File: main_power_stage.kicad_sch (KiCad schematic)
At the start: 67 parts, among them SW1 CAS-120TA, U2 LV14540DDAR, U6 TPS65987DDHRSHR, U7 LV14540DDAR, U8 74CBTLV3257_VQFN, U9 W25Q80DV_SOIC-8

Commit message: [#62623] Minor graphical changes
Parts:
- added R63: R_0R_0402, antmicro-footprints:R_0402_1005Metric, symbol antmicroResistors0402:R_0R_0402
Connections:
- net FTDI_TPS_rst: now also R63.1; no longer R32.2, U6.44 (HRESET)
- new net PDC_RESET: R32.2, R63.2, U6.44 (HRESET)
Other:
- moved on the sheet: R57, U8

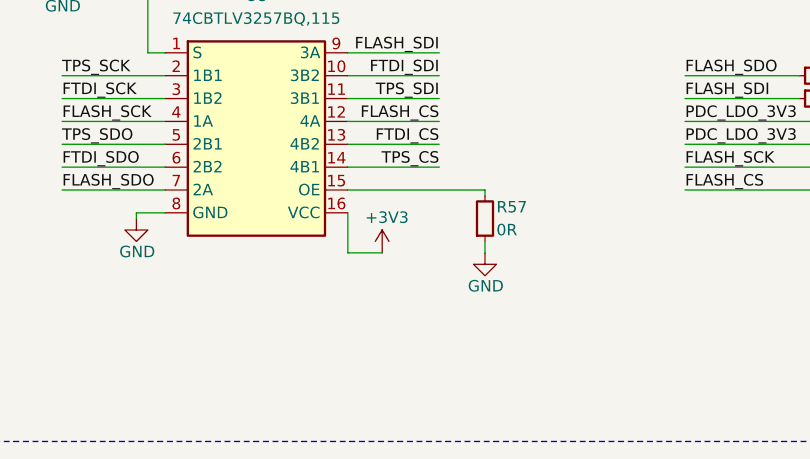
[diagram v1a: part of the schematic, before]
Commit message: [#62623] PCB initial placement
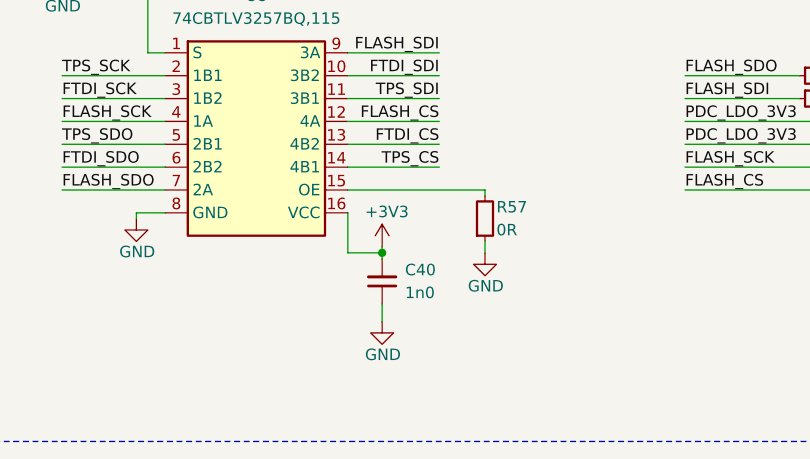
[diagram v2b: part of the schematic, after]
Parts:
- added C40: C_1n0_0402, antmicro-footprints:C_0402_1005Metric, symbol antmicroCapacitors0402:C_1n0_0402
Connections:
- net +3V3: now also C40.2
- net GND: now also C40.1
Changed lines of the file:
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@@
   (junction (at 154.305 92.71) (diameter 0) (color 0 0 0 0)
   )
+  (junction (at 147.32 263.525) (diameter 0) (color 0 0 0 0)
+  )
   (junction (at 247.65 96.52) (diameter 0) (color 0 0 0 0)
   )
@@
     (stroke (width 0) (type default))
   )
+  (wire (pts (xy 147.32 263.525) (xy 147.32 262.89))
+    (stroke (width 0) (type default))
+  )
   (wire (pts (xy 93.345 33.02) (xy 97.79 33.02))
     (stroke (width 0) (type default))
@@
     (stroke (width 0) (type default))
   )
-  (wire (pts (xy 143.51 259.08) (xy 143.51 263.525))
-    (stroke (width 0) (type default))
-  )
   (wire (pts (xy 257.81 96.52) (xy 261.62 96.52))
     (stroke (width 0) (type default))
@@
     (stroke (width 0) (type default))
   )
+  (wire (pts (xy 143.51 259.08) (xy 143.51 263.525))
+    (stroke (width 0) (type default))
+  )
   (wire (pts (xy 97.79 38.1) (xy 102.235 38.1))
     (stroke (width 0) (type default))
@@
     (stroke (width 0) (type default))
   )
+  (wire (pts (xy 143.51 263.525) (xy 147.32 263.525))
+    (stroke (width 0) (type default))
+  )
   (wire (pts (xy 252.73 69.215) (xy 252.73 70.485))
     (stroke (width 0) (type default))
@@
     (stroke (width 0) (type default))
   )
-  (wire (pts (xy 143.51 263.525) (xy 147.32 263.525))
+  (wire (pts (xy 147.32 264.16) (xy 147.32 263.525))
     (stroke (width 0) (type default))
   )
@@
     (stroke (width 0) (type default))
   )
+  (wire (pts (xy 147.32 269.24) (xy 147.32 271.145))
+    (stroke (width 0) (type default))
+  )
   (wire (pts (xy 128.27 152.4) (xy 128.27 154.94))
     (stroke (width 0) (type default))
@@
     (effects (font (size 1.27 1.27)) (justify right bottom))
   )
-  (label "SCL" (at 398.78 39.37 180)
+  (label "SCL" (at 398.78 39.37 180) (fields_autoplaced)
     (effects (font (size 1.27 1.27)) (justify right bottom))
   )
@@
     (effects (font (size 1.27 1.27)) (justify right bottom))
   )
-  (label "SDA" (at 398.78 41.91 180)
+  (label "SDA" (at 398.78 41.91 180) (fields_autoplaced)
     (effects (font (size 1.27 1.27)) (justify right bottom))
   )
@@
     (pin "8")
     (pin "7")
+    (pin "17")
     (instances
       (project "antmicro-poe-to-usbc-pd-adapter"
@@
     )
   )
+  (symbol (lib_id "antmicroCapacitors0402:C_1n0_0402") (at 147.32 269.24 90) (unit 1)
+    (in_bom yes) (on_board yes) (dnp no) (fields_autoplaced)
+    (property "Reference" "C40" (at 149.86 265.4236 90)
+      (effects (font (size 1.27 1.27) (thickness 0.15)) (justify right))
+    )
+    (property "Value" "C_1n0_0402" (at 157.48 248.92 0)
+      (effects (font (size 1.27 1.27) (thickness 0.15)) (justify left bottom) hide)
+    )
+    (property "Footprint" "antmicro-footprints:C_0402_1005Metric" (at 160.02 248.92 0)
+      (effects (font (size 1.27 1.27) (thickness 0.15)) (justify left bottom) hide)
+    )
+    (property "Datasheet" "https://www.we-online.com/components/products/datasheet/885012005018.pdf" (at 162.56 248.92 0)
+      (effects (font (size 1.27 1.27) (thickness 0.15)) (justify left bottom) hide)
+    )
+    (property "MPN" "885012005018" (at 165.1 248.92 0)
+      (effects (font (size 1.27 1.27) (thickness 0.15)) (justify left bottom) hide)
+    )
+    (property "Manufacturer" "Würth Elektronik" (at 167.64 248.92 0)
+      (effects (font (size 1.27 1.27) (thickness 0.15)) (justify left bottom) hide)
+    )
+    (property "License" "Apache-2.0" (at 170.18 248.92 0)
+      (effects (font (size 1.27 1.27) (thickness 0.15)) (justify left bottom) hide)
+    )
+    (property "Author" "Antmicro" (at 172.72 248.92 0)
+      (effects (font (size 1.27 1.27) (thickness 0.15)) (justify left bottom) hide)
+    )
+    (property "Val" "1n0" (at 149.86 267.9636 90)
+      (effects (font (size 1.27 1.27) (thickness 0.15)) (justify right))
+    )
+    (property "Voltage" "" (at 175.26 248.92 0)
+      (effects (font (size 1.27 1.27)) (justify left bottom) hide)
+    )
+    (property "Dielectric" "" (at 177.8 248.92 0)
+      (effects (font (size 1.27 1.27)) (justify left bottom) hide)
+    )
+    (pin "1")
+    (pin "2")
+    (instances
+      (project "antmicro-poe-to-usbc-pd-adapter"
+        (path "/cf0d4429-3f03-449f-96a7-26d69371a46d/47a421e3-70a1-4c86-94f4-557263ac6525"
+          (reference "C40") (unit 1)
+        )
+      )
+    )
+  )
   (symbol (lib_id "antmicropower:GND") (at 53.34 154.94 0) (unit 1)
     (in_bom yes) (on_board yes) (dnp no) (fields_autoplaced)
@@
     )
   )
-  (symbol (lib_id "antmicropower:+3V3") (at 147.32 263.525 0) (unit 1)
+  (symbol (lib_id "antmicropower:+3V3") (at 147.32 262.89 0) (unit 1)
     (in_bom yes) (on_board yes) (dnp no)
-    (property "Reference" "#PWR067" (at 147.32 267.335 0)
+    (property "Reference" "#PWR067" (at 147.32 266.7 0)
       (effects (font (size 1.27 1.27)) (justify left bottom) hide)
     )
-    (property "Value" "+3V3" (at 145.415 260.35 0)
+    (property "Value" "+3V3" (at 145.415 259.715 0)
       (effects (font (size 1.27 1.27)) (justify left bottom))
     )
-    (property "Footprint" "" (at 147.32 263.525 0)
+    (property "Footprint" "" (at 147.32 262.89 0)
       (effects (font (size 1.27 1.27)) (justify left bottom) hide)
     )
-    (property "Datasheet" "" (at 147.32 263.525 0)
+    (property "Datasheet" "" (at 147.32 262.89 0)
       (effects (font (size 1.27 1.27)) (justify left bottom) hide)
     )
@@
     )
   )
-  (symbol (lib_id "antmicroResistors0402:R_100k_0402") (at 252.73 96.52 0) (unit 1)
+  (symbol (lib_name "R_100k_0402_1") (lib_id "antmicroResistors0402:R_100k_0402") (at 252.73 96.52 0) (unit 1)
     (in_bom yes) (on_board yes) (dnp no)
     (property "Reference" "R28" (at 250.825 95.25 0)
@@
     )
   )
-  (symbol (lib_name "R_10k_0402_1") (lib_id "antmicroResistors0402:R_10k_0402") (at 254.635 87.63 0) (unit 1)
+  (symbol (lib_name "R_10k_0402_2") (lib_id "antmicroResistors0402:R_10k_0402") (at 254.635 87.63 0) (unit 1)
     (in_bom yes) (on_board yes) (dnp no) (fields_autoplaced)
     (property "Reference" "R32" (at 257.175 81.28 0)
@@
     )
   )
-  (symbol (lib_id "antmicroCapacitors0402:C_100n_0402") (at 241.3 64.135 270) (unit 1)
+  (symbol (lib_name "C_100n_0402_1") (lib_id "antmicroCapacitors0402:C_100n_0402") (at 241.3 64.135 270) (unit 1)
     (in_bom yes) (on_board yes) (dnp no)
     (property "Reference" "C26" (at 241.3 65.405 90)
@@
     )
   )
-  (symbol (lib_id "antmicroResistors0402:R_10k_0402") (at 252.73 107.95 0) (unit 1)
+  (symbol (lib_name "R_10k_0402_1") (lib_id "antmicroResistors0402:R_10k_0402") (at 252.73 107.95 0) (unit 1)
     (in_bom yes) (on_board yes) (dnp no)
     (property "Reference" "R30" (at 251.46 106.68 0)
@@
     )
   )
+  (symbol (lib_id "antmicropower:GND") (at 147.32 271.145 0) (unit 1)
+    (in_bom yes) (on_board yes) (dnp no)
+    (property "Reference" "#PWR087" (at 147.32 277.495 0)
+      (effects (font (size 1.27 1.27)) (justify left bottom) hide)
+    )
+    (property "Value" "GND" (at 145.415 275.59 0)
+      (effects (font (size 1.27 1.27)) (justify left bottom))
+    )
+    (property "Footprint" "" (at 147.32 271.145 0)
+      (effects (font (size 1.27 1.27)) (justify left bottom) hide)
+    )
+    (property "Datasheet" "" (at 147.32 271.145 0)
+      (effects (font (size 1.27 1.27)) (justify left bottom) hide)
+    )
+    (property "Author" "Antmicro" (at 156.21 278.765 0)
+      (effects (font (size 1.27 1.27) (thickness 0.15)) (justify left bottom) hide)
+    )
+    (property "License" "Apache-2.0" (at 156.21 281.305 0)
+      (effects (font (size 1.27 1.27) (thickness 0.15)) (justify left bottom) hide)
+    )
+    (pin "1")
+    (instances
+      (project "antmicro-poe-to-usbc-pd-adapter"
+        (path "/cf0d4429-3f03-449f-96a7-26d69371a46d/47a421e3-70a1-4c86-94f4-557263ac6525"
+          (reference "#PWR087") (unit 1)
+        )
+      )
+    )
+  )
   (symbol (lib_id "antmicroResistors0402:R_2k7_0402") (at 154.305 81.28 90) (unit 1)
     (in_bom yes) (on_board yes) (dnp no)
@@
     )
   )
-  (symbol (lib_id "antmicroDCDCConverters:LV14540DDAR") (at 83.82 139.7 0) (unit 1)
+  (symbol (lib_name "LV14540DDAR_1") (lib_id "antmicroDCDCConverters:LV14540DDAR") (at 83.82 139.7 0) (unit 1)
     (in_bom yes) (on_board yes) (dnp no) (fields_autoplaced)
     (property "Reference" "U7" (at 93.345 133.35 0)

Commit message: [#62623] Las commit before major change in placement
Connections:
- net FB1: now also U6.43 (GPIO15); no longer U6.40 (GPIO12)
- net FB2: now also U6.42 (GPIO14); no longer U6.41 (GPIO13)
- net FB3: now also U6.41 (GPIO13); no longer U6.42 (GPIO14)
- net FB4: now also U6.40 (GPIO12); no longer U6.43 (GPIO15)
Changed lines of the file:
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@@
     (effects (font (size 1.27 1.27)) (justify right bottom))
   )
-  (label "FB3" (at 313.69 113.03 180) (fields_autoplaced)
+  (label "FB3" (at 313.69 110.49 180) (fields_autoplaced)
     (effects (font (size 1.27 1.27)) (justify right bottom))
   )
@@
     (effects (font (size 1.27 1.27)) (justify left bottom))
   )
-  (label "FB2" (at 313.69 110.49 180) (fields_autoplaced)
+  (label "FB2" (at 313.69 113.03 180) (fields_autoplaced)
     (effects (font (size 1.27 1.27)) (justify right bottom))
   )
@@
     (effects (font (size 1.27 1.27)) (justify right bottom))
   )
-  (label "FB4" (at 313.69 115.57 180) (fields_autoplaced)
+  (label "FB4" (at 313.69 107.95 180) (fields_autoplaced)
     (effects (font (size 1.27 1.27)) (justify right bottom))
   )
@@
     (effects (font (size 1.27 1.27)) (justify right bottom))
   )
-  (label "FB1" (at 313.69 107.95 180) (fields_autoplaced)
+  (label "FB1" (at 313.69 115.57 180) (fields_autoplaced)
     (effects (font (size 1.27 1.27)) (justify right bottom))
   )
